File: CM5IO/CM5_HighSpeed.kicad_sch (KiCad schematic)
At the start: 17 parts, among them J12 USB3_A, J16 Conn_01x22_Female, J22 46765-1301, J5 Conn_01x22_Female, U12 RT9742SNGV, U6 AP22653W6

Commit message: move bottom board into CM5IO
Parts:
- added TP10: TP VBUS_HDMI, TestPoint:TestPoint_Pad_2.0x2.0mm, symbol Connector:TestPoint
- added TP9: TP VBUS_USB, TestPoint:TestPoint_Pad_2.0x2.0mm, symbol Connector:TestPoint
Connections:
- net HDMI_5v: now also TP10.1
- net VBUS: now also TP9.1

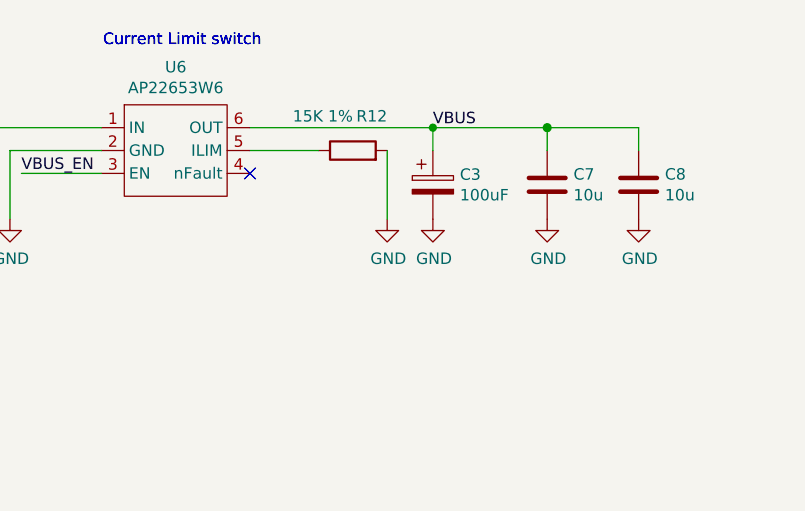
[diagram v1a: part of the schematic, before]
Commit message: DRC fixes after changing via size. fixed too small cap in PSU.
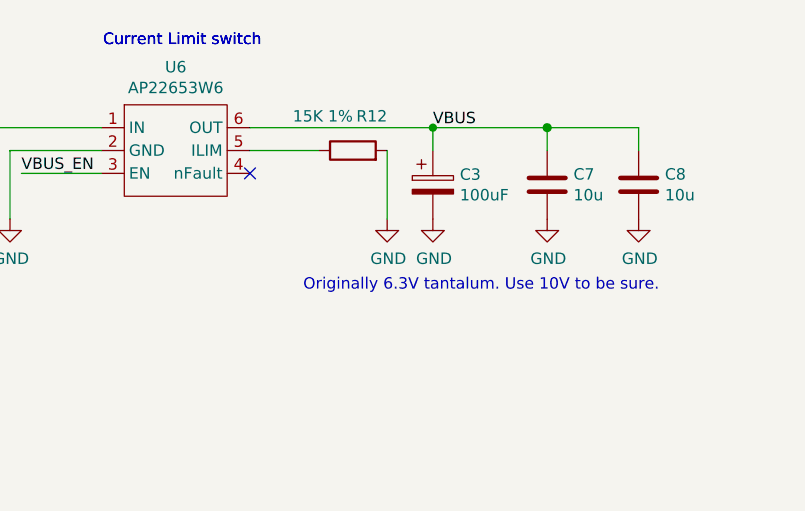
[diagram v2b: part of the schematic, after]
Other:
- note added: "Originally 6.3V tantalum. Use 10V to be sure."
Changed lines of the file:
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@@
+		)
+	)
+	(text "Originally 6.3V tantalum. Use 10V to be sure.\n"
+		(exclude_from_sim no)
+		(at 267.716 159.258 0)
+		(effects
+			(font
+				(size 1.27 1.27)
+			)
+			(justify right bottom)
 		)
 	)

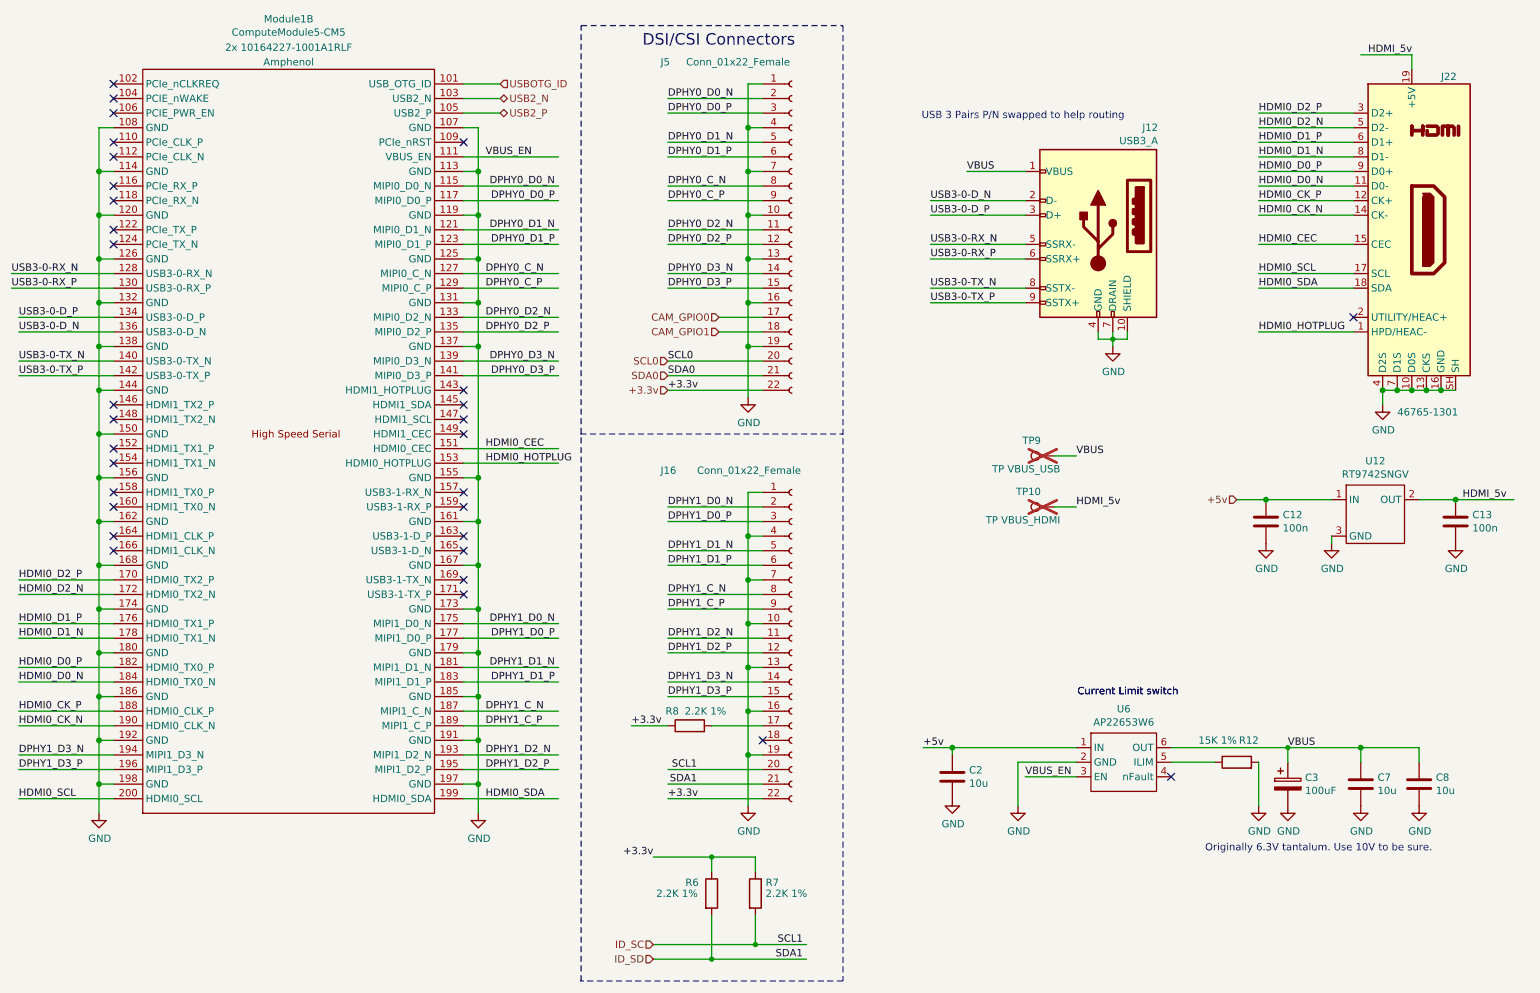
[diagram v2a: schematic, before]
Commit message: Add PCIe connector. Fix some clearance violations.
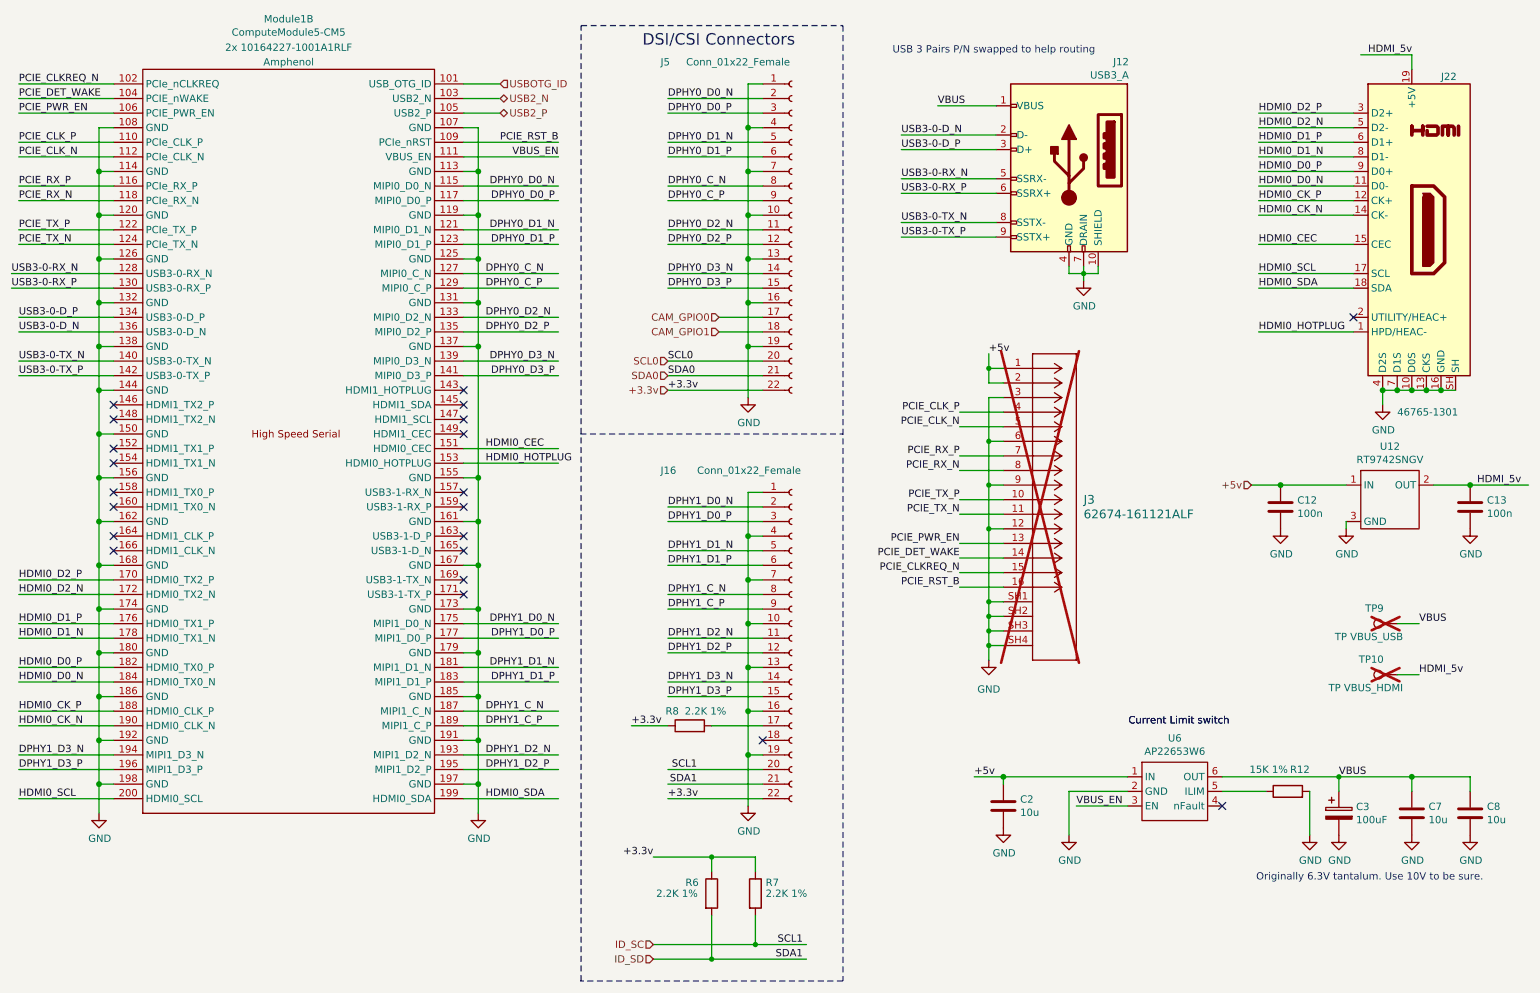
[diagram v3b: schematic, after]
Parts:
- added J3: 62674-161121ALF, CON16_1X16_DUT_58XF_GLE, symbol CM5IO:62674-161121ALF
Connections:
- net +5v: now also J3.1, J3.2
- net GND: now also J3.12, J3.3, J3.6, J3.9, J3.SH1, J3.SH2, J3.SH3, J3.SH4
- net PCIE_CLKREQ_N: now reaches Module1.102 (PCIe_nCLKREQ)
- net PCIE_CLKREQ_N: now also J3.15
- net PCIE_DET_WAKE: now reaches Module1.104 (PCIE_nWAKE)
- net PCIE_DET_WAKE: now also J3.14
- net PCIE_PWR_EN: now reaches Module1.106 (PCIE_PWR_EN)
- net PCIE_PWR_EN: now also J3.13
- net PCIE_RST_B: now reaches Module1.109 (PCIe_nRST)
- net PCIE_RST_B: now also J3.16
- net PCIE_CLK_P: now reaches Module1.110 (PCIe_CLK_P)
- net PCIE_CLK_P: now also J3.4
- net PCIE_CLK_N: now reaches Module1.112 (PCIe_CLK_N)
- net PCIE_CLK_N: now also J3.5
- net PCIE_RX_P: now reaches Module1.116 (PCIe_RX_P)
- net PCIE_RX_P: now also J3.7
- net PCIE_RX_N: now reaches Module1.118 (PCIe_RX_N)
- net PCIE_RX_N: now also J3.8
- net PCIE_TX_P: now reaches Module1.122 (PCIe_TX_P)
- net PCIE_TX_P: now also J3.10
- net PCIE_TX_N: now reaches Module1.124 (PCIe_TX_N)
- net PCIE_TX_N: now also J3.11
- no-connect marks 31 -> 21
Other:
- moved on the sheet: C12, C13, C2, C3, C7, C8, J12, R12, TP10, TP9, U12, U6
